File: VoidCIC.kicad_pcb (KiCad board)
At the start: 2 copper layers, 11.5 x 23 mm, 8 parts, among them U1 SN74LVC1GU04DBVR

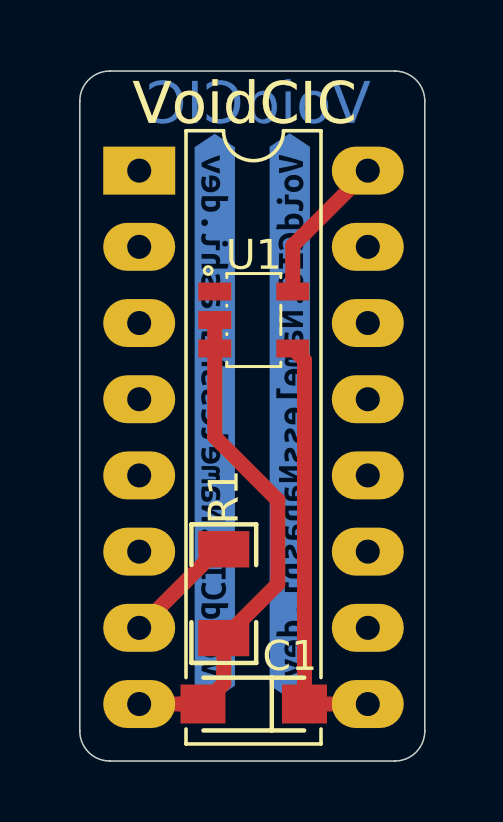
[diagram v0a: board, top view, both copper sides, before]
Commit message: Round tracks.
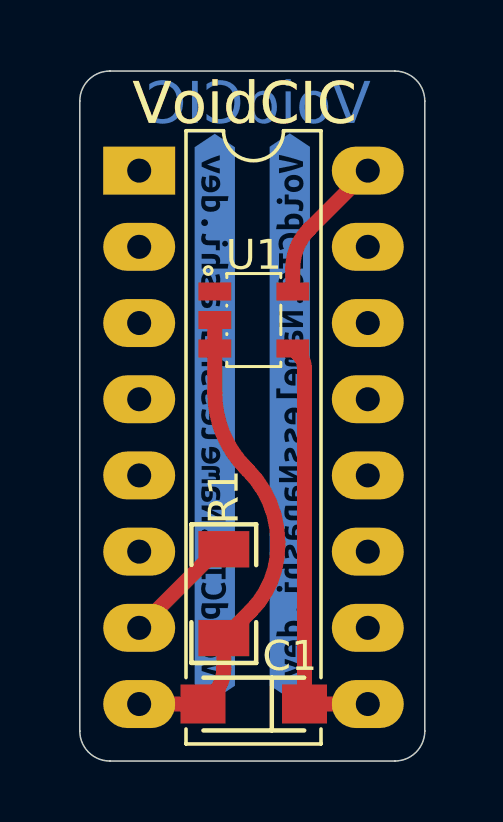
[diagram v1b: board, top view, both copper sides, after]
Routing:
- net GND: track 16.8 -> 16.2 mm
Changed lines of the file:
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@@
 	)
 	(segment
-		(start 182.1 93.85)
-		(end 182.1 92.32)
+		(start 182.1 93.085)
+		(end 182.1 93.85)
 		(width 0.5)
 		(layer "F.Cu")
@@
 	)
 	(segment
-		(start 182.1 92.32)
+		(start 182.640936 91.779063)
 		(end 184.6 89.82)
 		(width 0.5)
@@
 		(net 1)
 	)
-	(segment
-		(start 182.1 95.75)
-		(end 182.49 96.14)
-		(width 0.5)
-		(layer "F.Cu")
-		(net 3)
-	)
-	(segment
-		(start 184.6 107.6)
+	(arc
+		(start 182.640936 91.779063)
+		(mid 182.240584 92.378232)
+		(end 182.1 93.085)
+		(width 0.5)
+		(layer "F.Cu")
+		(net 1)
+	)
+	(segment
+		(start 182.295 95.945)
+		(end 182.1 95.75)
+		(width 0.5)
+		(layer "F.Cu")
+		(net 3)
+	)
+	(segment
+		(start 182.49 107.6)
+		(end 184.6 107.6)
+		(width 0.5)
+		(layer "F.Cu")
+		(net 3)
+	)
+	(segment
+		(start 182.49 96.415771)
 		(end 182.49 107.6)
 		(width 0.5)
@@
 		(net 3)
 	)
-	(segment
-		(start 182.49 96.14)
-		(end 182.49 107.6)
-		(width 0.5)
-		(layer "F.Cu")
-		(net 3)
-	)
-	(segment
-		(start 179.6 102.44)
+	(arc
+		(start 182.295 95.945)
+		(mid 182.439321 96.160991)
+		(end 182.49 96.415771)
+		(width 0.5)
+		(layer "F.Cu")
+		(net 3)
+	)
+	(segment
+		(start 179.529289 102.51071)
 		(end 176.98 105.06)
 		(width 0.5)
@@
 	)
 	(segment
-		(start 179.8 102.44)
-		(end 179.6 102.44)
+		(start 179.7 102.44)
+		(end 179.8 102.44)
 		(width 0.5)
 		(layer "F.Cu")
 		(net 4)
 	)
-	(segment
-		(start 179.5 98.7)
+	(arc
+		(start 179.7 102.44)
+		(mid 179.607611 102.458376)
+		(end 179.529289 102.51071)
+		(width 0.5)
+		(layer "F.Cu")
+		(net 4)
+	)
+	(segment
+		(start 179.5 97.225)
 		(end 179.5 95.75)
 		(width 0.5)
@@
 	)
 	(segment
-		(start 179.11 107.6)
+		(start 178.622096 107.6)
 		(end 176.98 107.6)
 		(width 0.5)
@@
 	)
 	(segment
-		(start 181.6 100.8)
-		(end 179.5 98.7)
-		(width 0.5)
-		(layer "F.Cu")
-		(net 5)
-	)
-	(segment
-		(start 179.5 94.8)
-		(end 179.5 95.75)
-		(width 0.5)
-		(layer "F.Cu")
-		(net 5)
-	)
-	(segment
-		(start 179.8 105.4)
-		(end 179.8 106.91)
-		(width 0.5)
-		(layer "F.Cu")
-		(net 5)
-	)
-	(segment
-		(start 179.8 105.4)
-		(end 181.6 103.6)
-		(width 0.5)
-		(layer "F.Cu")
-		(net 5)
-	)
-	(segment
-		(start 179.8 106.91)
-		(end 179.11 107.6)
-		(width 0.5)
-		(layer "F.Cu")
-		(net 5)
-	)
-	(segment
-		(start 181.6 103.6)
-		(end 181.6 100.8)
-		(width 0.5)
-		(layer "F.Cu")
-		(net 5)
-	)
-	(zone
-		(net 5)
-		(net_name "GND")
-		(layer "F.Cu")
-		(name "$teardrop_padvia$")
-		(hatch full 0.1)
-		(priority 30002)
-		(attr
-			(teardrop
-				(type padvia)
-			)
-		)
-		(connect_pads yes
-			(clearance 0)
-		)
-		(min_thickness 0.0254)
-		(filled_areas_thickness no)
-		(fill yes
-			(thermal_gap 0.5)
-			(thermal_bridge_width 0.5)
-			(island_removal_mode 1)
-			(island_area_min 10)
-		)
-		(polygon
-			(pts
-				(xy 178.943567 107.41288) (xy 178.57053 107.345194) (xy 178.197493 107.185842) (xy 177.824456 106.934824)
-				(xy 176.979293 107.600707) (xy 177.536072 108.384628) (xy 178.123088 108.086896) (xy 178.710104 107.880831)
-				(xy 179.29712 107.766433)
-			)
-		)
+		(start 180.61005 99.81005)
+		(end 180.542982 99.742982)
+		(width 0.5)
+		(layer "F.Cu")
+		(net 5)
+	)
+	(segment
+		(start 179.5 95.75)
+		(end 179.5 94.8)
+		(width 0.5)
+		(layer "F.Cu")
+		(net 5)
+	)
+	(segment
+		(start 179.8 106.422096)
+		(end 179.8 105.4)
+		(width 0.5)
+		(layer "F.Cu")
+		(net 5)
+	)
+	(segment
+		(start 180.7 104.5)
+		(end 179.8 105.4)
+		(width 0.5)
+		(layer "F.Cu")
+		(net 5)
+	)
+	(segment
+		(start 181.6 102.2)
+		(end 181.6 102.327207)
+		(width 0.5)
+		(layer "F.Cu")
+		(net 5)
+	)
+	(arc
+		(start 179.455 107.255)
+		(mid 179.07286 107.510337)
+		(end 178.622096 107.6)
+		(width 0.5)
+		(layer "F.Cu")
+		(net 5)
+	)
+	(arc
+		(start 179.8 106.422096)
+		(mid 179.710337 106.87286)
+		(end 179.455 107.255)
+		(width 0.5)
+		(layer "F.Cu")
+		(net 5)
+	)
+	(arc
+		(start 180.61005 99.81005)
+		(mid 181.34272 100.906568)
+		(end 181.6 102.2)
+		(width 0.5)
+		(layer "F.Cu")
+		(net 5)
+	)
+	(arc
+		(start 181.6 102.327207)
+		(mid 181.366097 103.503114)
+		(end 180.7 104.5)
+		(width 0.5)
+		(layer "F.Cu")
+		(net 5)
+	)
+	(arc
+		(start 179.5 97.225)
+		(mid 179.771062 98.587722)
+		(end 180.542982 99.742982)
+		(width 0.5)
+		(layer "F.Cu")
+		(net 5)
 	)
 	(zone
@@
 				(xy 179.25 95.09) (xy 179.233333 95.218333) (xy 179.216666 95.338333) (xy 179.2 95.45) (xy 179.5 95.751)
 				(xy 179.8 95.45) (xy 179.783333 95.338333) (xy 179.766666 95.218333) (xy 179.75 95.09)
+			)
+		)
+	)
+	(zone
+		(net 5)
+		(net_name "GND")
+		(layer "F.Cu")
+		(name "$teardrop_padvia$")
+		(hatch full 0.1)
+		(priority 30001)
+		(attr
+			(teardrop
+				(type padvia)
+			)
+		)
+		(connect_pads yes
+			(clearance 0)
+		)
+		(min_thickness 0.0254)
+		(filled_areas_thickness no)
+		(fill yes
+			(thermal_gap 0.5)
+			(thermal_bridge_width 0.5)
+			(island_removal_mode 1)
+			(island_area_min 10)
+		)
+		(polygon
+			(pts
+				(xy 179.55 106.184913) (xy 179.268049 106.506608) (xy 178.986099 106.761637) (xy 178.704149 106.95)
+				(xy 179.11 107.601) (xy 179.86 107.545703) (xy 179.923333 107.025439) (xy 179.986666 106.571843)
+				(xy 180.05 106.184913)
 			)
 		)
@@
 	)
 	(zone
-		(net 5)
-		(net_name "GND")
-		(layer "F.Cu")
-		(name "$teardrop_padvia$")
-		(hatch full 0.1)
-		(priority 30005)
-		(attr
-			(teardrop
-				(type padvia)
-			)
-		)
-		(connect_pads yes
-			(clearance 0)
-		)
-		(min_thickness 0.0254)
-		(filled_areas_thickness no)
-		(fill yes
-			(thermal_gap 0.5)
-			(thermal_bridge_width 0.5)
-			(island_removal_mode 1)
-			(island_area_min 10)
-		)
-		(polygon
-			(pts
-				(xy 179.55 106.186568) (xy 179.268119 106.507711) (xy 178.986238 106.762189) (xy 178.704358 106.95)
-				(xy 179.11 107.601) (xy 179.86 107.5461) (xy 179.923333 107.026256) (xy 179.986666 106.573078) (xy 180.05 106.186568)
-			)
-		)
-	)
-	(zone
-		(net 4)
-		(net_name "RST IN")
-		(layer "F.Cu")
-		(name "$teardrop_padvia$")
-		(hatch full 0.1)
-		(priority 30000)
-		(attr
-			(teardrop
-				(type padvia)
-			)
-		)
-		(connect_pads yes
-			(clearance 0)
-		)
-		(min_thickness 0.0254)
-		(filled_areas_thickness no)
-		(fill yes
-			(thermal_gap 0.5)
-			(thermal_bridge_width 0.5)
-			(island_removal_mode 1)
-			(island_area_min 10)
-		)
-		(polygon
-			(pts
-				(xy 178.658418 103.735136) (xy 179.112923 103.445924) (xy 179.567428 103.215878) (xy 180.021934 103.045)
-				(xy 179.800707 102.439293) (xy 178.95 102.367622) (xy 178.734954 102.764775) (xy 178.519909 103.102761)
-				(xy 178.304864 103.381582)
+		(net 3)
+		(net_name "RST OUT")
+		(layer "F.Cu")
+		(name "$teardrop_padvia$")
+		(hatch full 0.1)
+		(priority 30003)
+		(attr
+			(teardrop
+				(type padvia)
+			)
+		)
+		(connect_pads yes
+			(clearance 0)
+		)
+		(min_thickness 0.0254)
+		(filled_areas_thickness no)
+		(fill yes
+			(thermal_gap 0.5)
+			(thermal_bridge_width 0.5)
+			(island_removal_mode 1)
+			(island_area_min 10)
+		)
+		(polygon
+			(pts
+				(xy 182.739589 96.38681) (xy 182.704314 96.282873) (xy 182.66904 96.170603) (xy 182.633766 96.05)
+				(xy 182.099985 95.749001) (xy 181.931791 96.05) (xy 182.03441 96.156461) (xy 182.137029 96.271255)
+				(xy 182.239648 96.394384)
 			)
 		)
@@
 	)
 	(zone
+		(net 5)
+		(net_name "GND")
+		(layer "F.Cu")
+		(name "$teardrop_padvia$")
+		(hatch full 0.1)
+		(priority 30002)
+		(attr
+			(teardrop
+				(type padvia)
+			)
+		)
+		(connect_pads yes
+			(clearance 0)
+		)
+		(min_thickness 0.0254)
+		(filled_areas_thickness no)
+		(fill yes
+			(thermal_gap 0.5)
+			(thermal_bridge_width 0.5)
+			(island_removal_mode 1)
+			(island_area_min 10)
+		)
+		(polygon
+			(pts
+				(xy 177.58 107.85) (xy 177.84 107.916666) (xy 178.1 108.05) (xy 178.36 108.25) (xy 179.111 107.6)
+				(xy 178.36 106.95) (xy 178.1 107.149999) (xy 177.84 107.283333) (xy 177.58 107.35)
+			)
+		)
+	)
+	(zone
 		(net 3)
 		(net_name "RST OUT")
@@
 	)
 	(zone
-		(net 3)
-		(net_name "RST OUT")
+		(net 4)
+		(net_name "RST IN")
 		(layer "F.Cu")
 		(name "$teardrop_padvia$")
@@
 		(polygon
 			(pts
-				(xy 182.74 96.372721) (xy 182.707342 96.27348) (xy 182.674685 96.165907) (xy 182.642028 96.05) (xy 182.1 95.749)
-				(xy 181.93439 96.05) (xy 182.03626 96.14924) (xy 182.13813 96.256813) (xy 182.24 96.372721)
-			)
-		)
+				(xy 178.658417 103.735136) (xy 179.112922 103.445924) (xy 179.567428 103.215878) (xy 180.021934 103.045)
+				(xy 179.800707 102.439293) (xy 178.95 102.367622) (xy 178.734954 102.764775) (xy 178.519908 103.102761)
+				(xy 178.304863 103.381582)
+			)
+		)

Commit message: MAJOR FIX: Repair Schematic to actually be correct now, Redherring32's schematic was a nightmare so I double checked the board and noticed this issue.
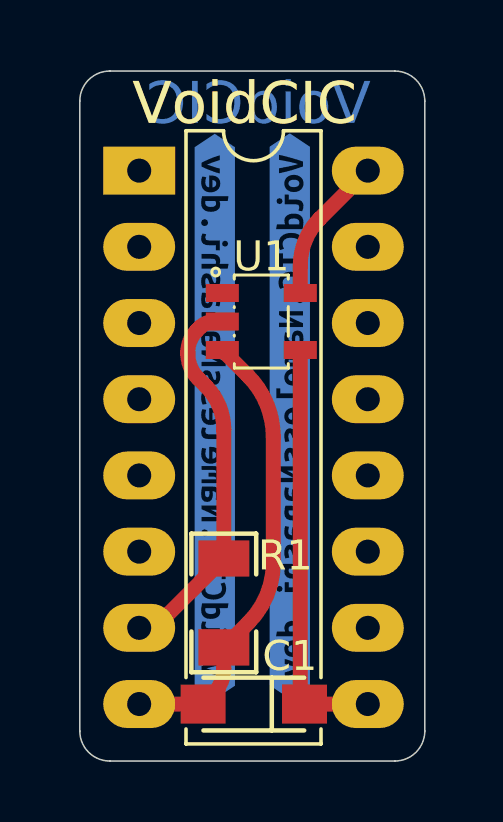
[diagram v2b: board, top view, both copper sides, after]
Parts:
- moved R1 0.31 mm to (179.8, 104.2)
- moved U1 0.25 mm to (181.1, 94.8)
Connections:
- U1 pad 2: GND -> RST IN
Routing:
- net RST IN: track 3.89 -> 12.7 mm
- net GND: track 16.2 -> 15.2 mm

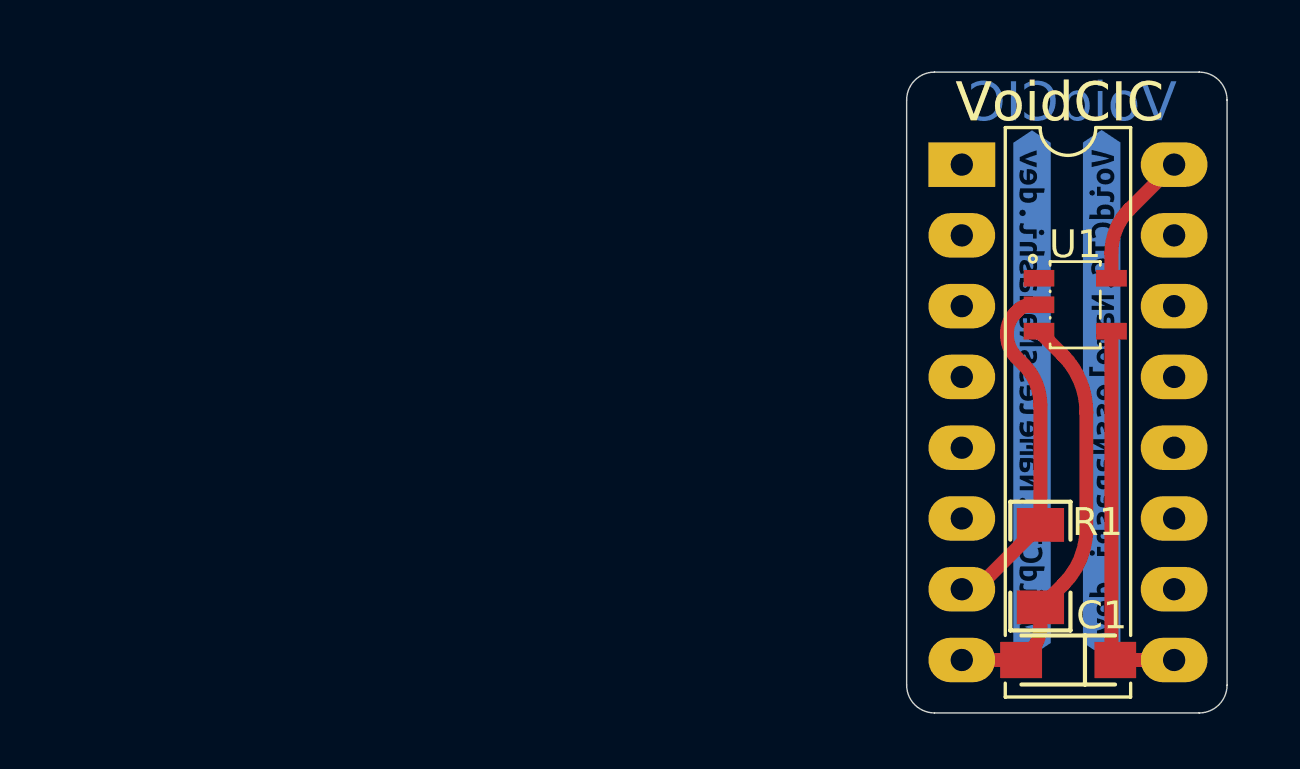
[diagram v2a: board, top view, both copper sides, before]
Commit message: update pcb and sch locations
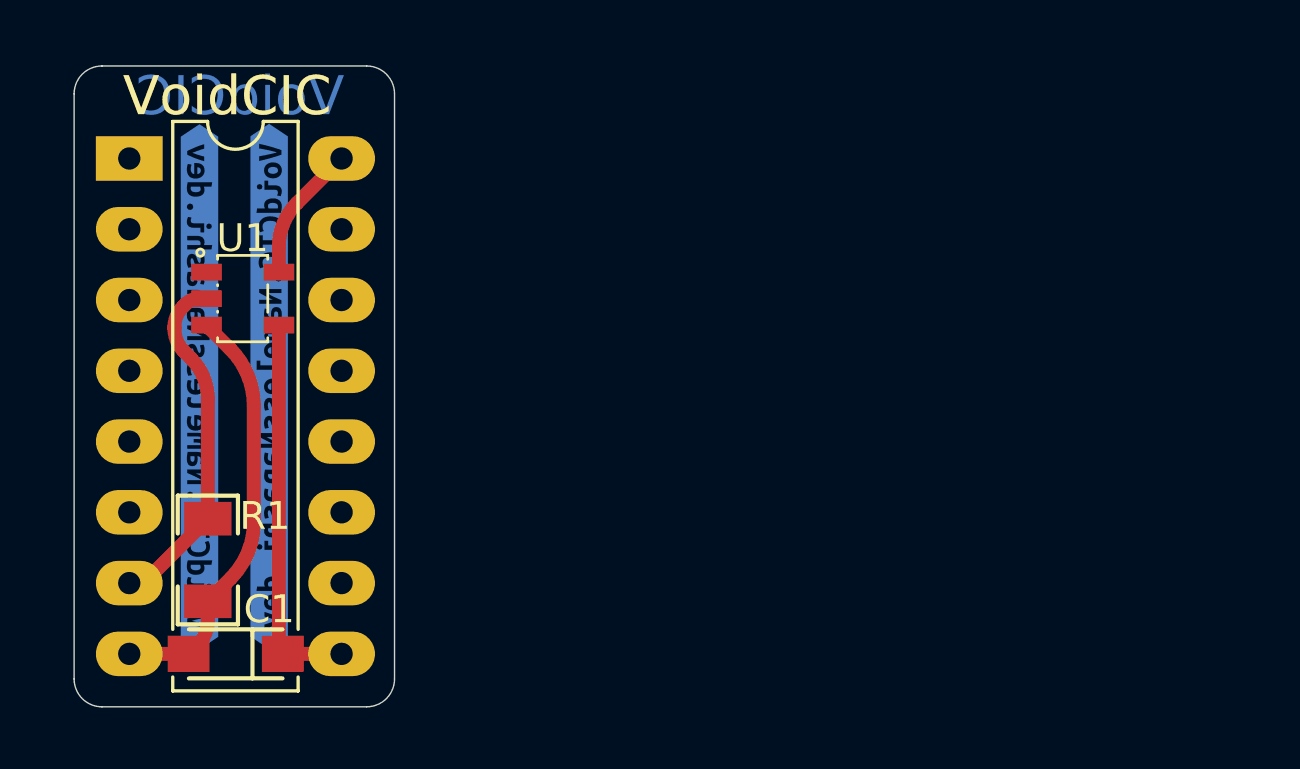
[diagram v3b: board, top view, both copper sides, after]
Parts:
- moved C1 29.9 mm to (150.9, 107.4)
- moved R1 29.9 mm to (149.9, 104.0)
- moved U1 29.9 mm to (151.2, 94.6)
- moved VoidCIC1 29.9 mm to (147.1, 89.6)
- moved kibuzzard-675A635B 29.9 mm to (152.1, 97.8)
- moved kibuzzard-675A635B 29.9 mm to (149.6, 97.8)
- moved kibuzzard-675A6399 29.9 mm to (152.1, 97.8)
- moved kibuzzard-675A6399 29.9 mm to (149.6, 97.8)

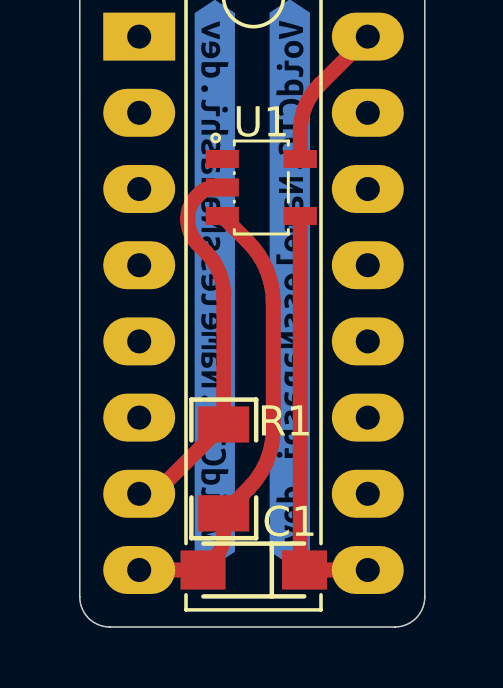
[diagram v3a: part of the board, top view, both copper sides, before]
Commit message: update production files to make soldering to easier
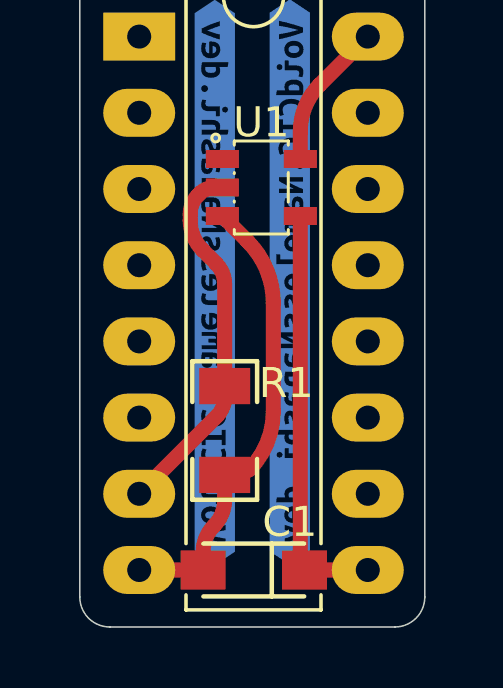
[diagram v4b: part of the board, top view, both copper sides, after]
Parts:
- moved R1 1.28 mm to (149.9, 102.7)
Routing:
- net GND: track 15.2 -> 14.5 mm
- net RST IN: track 12.7 -> 13.2 mm
